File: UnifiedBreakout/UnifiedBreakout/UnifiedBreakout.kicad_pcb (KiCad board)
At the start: 2 copper layers, 307.3 x 121.9 mm, 95 parts, among them J1 24V DC IN, J10 MESA P2 INTERNAL IO, J11 MESA P3 REAR IO, J12 ENCODER IN, J13 ENCODER OUT, J14 ARGON J5, J15 ARGON J2.2, J16 RJ14, J17 RJ14, J18 RJ14, J19 RJ14, J2 ATX-24, J20 RJ14, J21 PENDANT, J22 DRAWBAR, J23 MIST, J24 AXIS PWR IN, J25 AXIS PWR OUT, J3 5V BUS, J4 24V BUS, J5 12V BUS, J7 RJ45, J8 RJ45, J9 RJ45, Q1 BC547, Q2 BC547, Q3 BC547, U1 4N35, U2 4N35, U3 4N35, U4 4N35, U5 4N35, U6 4N35, U7 74HC14

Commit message: Updated BOM
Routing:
- net +24V: vias 2 -> 1

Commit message: Final updates to unified BoB
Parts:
- C1, C3, C5, C7: footprint Capacitor_THT:C_Disc_D5.0mm_W2.5mm_P2.50mm -> Capacitor_THT:C_Disc_D5.0mm_W2.5mm_P5.00mm
- D5: value AXIS PWR -> LED
- D7: value DRAWBAR -> LED
- D9: value MIST -> LED
- R1, R10, R11, R12, R13, R14, R15, R16, R17, R18, R19, R2, R20, R21, R22, R23, R24, R25, R26, R27, R28, R29, R3, R30, R31, R4, R5, R6, R7, R8, R9: footprint Resistor_THT:R_Axial_DIN0207_L6.3mm_D2.5mm_P10.16mm_Horizontal -> Resistor_THT:R_Axial_DIN0207_L6.3mm_D2.5mm_P7.62mm_Horizontal
- moved R14 2.67 mm to (7.49, 139.4)
- moved R16 2.54 mm to (7.37, 155.2)
- moved R18 2.54 mm to (7.37, 171.4)
- moved R20 2.54 mm to (7.37, 203.7)
- moved R27 2.54 mm to (22.9, 136.9)
- moved R28 2.54 mm to (22.9, 152.7)
- moved R29 2.54 mm to (22.9, 168.9)
- moved R30 2.54 mm to (22.9, 201.2)
- moved R22 2.41 mm to (7.49, 188.2)
- moved R31 2.29 mm to (23.1, 185.7)
- moved J22 1.27 mm to (243.7, 114.3)
- moved J23 1.27 mm to (228.9, 114.3)
- moved J12 0.64 mm to (17.8, 116.2)
- moved J13 0.64 mm to (59.7, 116.2)
- moved J16 0.63 mm to (-8.76, 134.4)
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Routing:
- net +12V: track 308.9 -> 250.8 mm
- net +5V: track 511.8 -> 566.6 mm
- net GND: track 0.00 -> 53.2 mm
- net /ARGON ENCODER/B-: track 47.0 -> 58.1 mm, vias 3 -> 0
- net /SPINDLE_PWM_DIR: track 203.4 -> 210.8 mm
- net /ESTOP: track 226.8 -> 223.1 mm, vias 2 -> 1
- net Net-(D4-Pad2): track 8.67 -> 11.2 mm
- net Net-(D2-Pad2): track 4.07 -> 6.61 mm
- net /MIST RELAY/ENABLE: track 16.5 -> 19.1 mm
- net /DRAWBAR RELAY/ENABLE: track 17.0 -> 19.6 mm
- net /AXIS POWER RELAY/ENABLE: track 18.6 -> 21.2 mm
- net /ARGON ENCODER/A-: track 45.1 -> 47.6 mm
- net Net-(D6-Pad2): track 16.1 -> 18.5 mm
- net +5VP: track 370.2 -> 372.6 mm
- net /ATX_PWR: track 230.4 -> 228.1 mm
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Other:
- net class 12V net added: clearance 0.5, trace_width 2, via_dia 1.5, via_drill 1

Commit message: Generate gerbers
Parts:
- D5: value LED -> AXIS PWR
- D7: value LED -> DRAWBAR
- D9: value LED -> MIST
- ENCODER PWR SEL: renamed from JP1
- moved J24 1.27 mm to (233.2, 217.4)
- moved J25 1.27 mm to (208.8, 217.4)
- moved J22 1.02 mm to (243.7, 115.3)
- moved J23 1.02 mm to (228.9, 115.3)
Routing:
- net /L_OUT: track 26.2 -> 25.0 mm
- net /N_IN: track 18.1 -> 16.9 mm
- net /N_OUT: track 79.2 -> 78.0 mm
- net /L_IN: track 19.0 -> 17.9 mm
- net /MIST RELAY/IN_A: track 11.8 -> 10.8 mm
- net /DRAWBAR RELAY/IN_A: track 12.0 -> 11.0 mm
- net +12V: track 250.8 -> 249.8 mm

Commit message: Update big breakout board to Kicad nightly
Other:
- net class 12V net removed
- net class Default removed
- net class ESTOP removed
- net class Gnd removed
- net class High power removed
- net class Low power removed
- net class Mains removed

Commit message: WIP updating breakout for electrical enclosure
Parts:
- removed C1, C5: 100n, Capacitor_THT:C_Disc_D5.0mm_W2.5mm_P5.00mm
- removed C2, C6: 100uF, Capacitor_THT:CP_Radial_D8.0mm_P3.50mm
- removed D10, D8: 1N4001, Diode_THT:D_DO-41_SOD81_P10.16mm_Horizontal
- removed D3: ATX PWR GOOD, LED_THT:LED_D3.0mm
- removed D4: ATX STBY, LED_THT:LED_D3.0mm
- removed D7: DRAWBAR, LED_THT:LED_D3.0mm
- removed D9: MIST, LED_THT:LED_D3.0mm
- removed ENCODER PWR SEL: ENCODER PWR SEL, Connector_PinHeader_2.54mm:PinHeader_1x03_P2.54mm_Vertical
- removed J16, J17, J18, J19, J20: RJ14, Wurth:615004141121
- removed J22: DRAWBAR, Connector_Phoenix_MSTB:PhoenixContact_MSTBA_2,5_2-G-5,08_1x02_P5.08mm_Horizontal
- removed J23: MIST, Connector_Phoenix_MSTB:PhoenixContact_MSTBA_2,5_2-G-5,08_1x02_P5.08mm_Horizontal
- removed J3: 5V BUS, Connector_Phoenix_MSTB:PhoenixContact_MSTBA_2,5_2-G-5,08_1x02_P5.08mm_Horizontal
- removed J5: 12V BUS, Connector_Phoenix_MSTB:PhoenixContact_MSTBA_2,5_2-G-5,08_1x02_P5.08mm_Horizontal
- removed Q3: BC547, Package_TO_SOT_THT:TO-92_Inline_Wide
- removed R11, R13: 680R, Resistor_THT:R_Axial_DIN0207_L6.3mm_D2.5mm_P7.62mm_Horizontal
- removed R12: 2K2, Resistor_THT:R_Axial_DIN0207_L6.3mm_D2.5mm_P7.62mm_Horizontal
- removed R25: 10K, Resistor_THT:R_Axial_DIN0207_L6.3mm_D2.5mm_P7.62mm_Horizontal
- removed RL2, RL3: JW2, Relay_THT:Relay_DPDT_Panasonic_JW2
- added Q4: 2N7000, Package_TO_SOT_THT:TO-92_Inline, F.Cu at (89.7, 82.3)
- added U9: 4N35, Package_DIP:DIP-6_W7.62mm, F.Cu at (162.8, 86.4)
- D5: value AXIS PWR -> LED
- J1: value 24V DC IN -> DRAWBAR+MIST; footprint SwitchCraft-BarrelJack-RAPC722BK:RAPC722BK -> Connector_Phoenix_MSTB:PhoenixContact_MSTBA_2,5_2-G-5,08_1x02_P5.08mm_Horizontal
- J2: value ATX-24 -> Screw_Terminal_01x05; footprint Connector_Molex:Molex_Mini-Fit_Jr_5569-24A2_2x12_P4.20mm_Horizontal -> Connector_Phoenix_MSTB:PhoenixContact_MSTBA_2,5_5-G-5,08_1x05_P5.08mm_Horizontal
- Q1: footprint Package_TO_SOT_THT:TO-92_Inline_Wide -> Package_TO_SOT_THT:TO-92_Inline
- Q2: value BC547 -> 2N7000; footprint Package_TO_SOT_THT:TO-92_Inline_Wide -> Package_TO_SOT_THT:TO-92_Inline
- R1, R10: value 2K2 -> 10K
- R4: value 220R -> 2K2
- R5: value 220R -> 220K
- moved J2 429.3 mm to (-149.9, 162.6), turned to 0 degrees
- moved J24 234.8 mm to (47.9, 73.2)
- moved H6 227.1 mm to (63.2, 65.8)
- moved C4 219.7 mm to (81.2, 78.0), turned to 0 degrees
- moved J4 218.6 mm to (71.1, 132.1), turned to 180 degrees
- moved J1 218.6 mm to (58.4, 165.1), turned to 0 degrees
- moved H3 209.8 mm to (55.2, 57.8)
- moved J25 206.7 mm to (47.9, 87.7)
- moved C3 206.0 mm to (79.5, 94.4), turned to 0 degrees
- moved R1 205.1 mm to (68.7, 75.3), turned to 0 degrees
- moved H4 205.0 mm to (55.2, 65.8)
- moved J15 203.5 mm to (12.2, 72.9)
- moved R22 169.9 mm to (149.9, 95.6)
- moved U6 169.5 mm to (149.9, 86.4)
- moved R20 168.9 mm to (137.0, 95.6)
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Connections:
- net /X MOT/DIR renamed /MESA P3 REAR IO/IO_04_STEPGEN_00_DIR
- net /Y MOT/DIR renamed /MESA P3 REAR IO/IO_08_STEPGEN_01_DIR
- net /Z MOT/DIR renamed /MESA P3 REAR IO/IO_10_STEPGEN_02_DIR
- D5 pad 2: +12V -> +24V
- D6 pad 1: +12V -> +24V
- J1 pad 1: +24V -> Net-(J1-Pin_1)
- J1 pad 2: GND -> Net-(J1-Pin_2)
- J10 pad 3: /ATX_PWR -> /TOOL_PROBE
- J12 pad 0: GND -> (no net)
- J12 pad 1: Net-(J12-Pad1) -> unconnected-(J12-Pad1)
- J12 pad 11: Net-(J12-Pad11) -> unconnected-(J12-P111-Pad11)
- J12 pad 12: Net-(J12-Pad12) -> unconnected-(J12-P12-Pad12)
- J12 pad 13: Net-(J12-Pad13) -> unconnected-(J12-P13-Pad13)
- J12 pad 2: Net-(J12-Pad2) -> unconnected-(J12-Pad2)
- J12 pad 3: Net-(J12-Pad3) -> unconnected-(J12-Pad3)
- J12 pad 4: Net-(J12-Pad4) -> unconnected-(J12-Pad4)
- J12 pad 9: Net-(J12-Pad9) -> Net-(J12-P9)
- J13 pad 0: GND -> (no net)
- J13 pad 1: Net-(J13-Pad1) -> unconnected-(J13-Pad1)
- J13 pad 11: Net-(J13-Pad11) -> unconnected-(J13-P111-Pad11)
- J13 pad 12: Net-(J13-Pad12) -> unconnected-(J13-P12-Pad12)
- J13 pad 13: Net-(J13-Pad13) -> unconnected-(J13-P13-Pad13)
- J13 pad 2: Net-(J13-Pad2) -> unconnected-(J13-Pad2)
- J13 pad 3: Net-(J13-Pad3) -> unconnected-(J13-Pad3)
- J13 pad 4: Net-(J13-Pad4) -> unconnected-(J13-Pad4)
- J13 pad 9: /ARGON ENCODER/ARGON5V -> Net-(J12-P9)
- J14 pad 10: Net-(J14-Pad10) -> unconnected-(J14-Pin_10-Pad10)
- J14 pad 11: Net-(J14-Pad11) -> unconnected-(J14-Pin_11-Pad11)
- J14 pad 12: Net-(J14-Pad12) -> unconnected-(J14-Pin_12-Pad12)
- J14 pad 13: Net-(J14-Pad13) -> unconnected-(J14-Pin_13-Pad13)
- J14 pad 14: Net-(J14-Pad14) -> unconnected-(J14-Pin_14-Pad14)
- J14 pad 17: Net-(J14-Pad17) -> unconnected-(J14-Pin_17-Pad17)
- J14 pad 18: Net-(J14-Pad18) -> unconnected-(J14-Pin_18-Pad18)
- J14 pad 19: Net-(J14-Pad19) -> unconnected-(J14-Pin_19-Pad19)
- J14 pad 2: Net-(J14-Pad2) -> unconnected-(J14-Pin_2-Pad2)
- J14 pad 20: Net-(J14-Pad20) -> unconnected-(J14-Pin_20-Pad20)
- J14 pad 21: Net-(J14-Pad21) -> unconnected-(J14-Pin_21-Pad21)
- J14 pad 22: Net-(J14-Pad22) -> unconnected-(J14-Pin_22-Pad22)
- J14 pad 23: Net-(J14-Pad23) -> unconnected-(J14-Pin_23-Pad23)
- J14 pad 24: Net-(J14-Pad24) -> unconnected-(J14-Pin_24-Pad24)
- J14 pad 25: Net-(J14-Pad25) -> unconnected-(J14-Pin_25-Pad25)
- J14 pad 26: Net-(J14-Pad26) -> unconnected-(J14-Pin_26-Pad26)
- J14 pad 3: Net-(J14-Pad3) -> unconnected-(J14-Pin_3-Pad3)
- J14 pad 5: Net-(J14-Pad5) -> unconnected-(J14-Pin_5-Pad5)
- J14 pad 7: Net-(J14-Pad7) -> unconnected-(J14-Pin_7-Pad7)
- J14 pad 8: Net-(J14-Pad8) -> unconnected-(J14-Pin_8-Pad8)
- J14 pad 9: Net-(J14-Pad9) -> unconnected-(J14-Pin_9-Pad9)
- J15 pad 2: Net-(J15-Pad2) -> unconnected-(J15-Pad2)
- J2 pad 1: Net-(J2-Pad1) -> /LIM X/INPUT
- J2 pad 2: Net-(J2-Pad1) -> /LIM Y/INPUT
- J2 pad 3: GND -> /LIM Z/INPUT
- J2 pad 4: +5V -> /PROBE/INPUT
- J2 pad 5: GND -> /TOOL_PROBE/INPUT
- J21 pad 10: Net-(J21-Pad10) -> unconnected-(J21-Pad10)
- J21 pad 13: Net-(J21-Pad13) -> unconnected-(J21-Pad13)
- J21 pad 17: Net-(J21-Pad17) -> unconnected-(J21-P17-Pad17)
- J21 pad 18: Net-(J21-Pad18) -> unconnected-(J21-P18-Pad18)
- J21 pad 22: Net-(J21-Pad22) -> unconnected-(J21-P22-Pad22)
- J21 pad 23: Net-(J21-Pad23) -> unconnected-(J21-P23-Pad23)
- J21 pad 24: Net-(J21-Pad24) -> unconnected-(J21-P24-Pad24)
- J21 pad 6: Net-(J21-Pad6) -> unconnected-(J21-Pad6)
- J21 pad 7: Net-(J21-Pad7) -> unconnected-(J21-Pad7)
- J21 pad 8: Net-(J21-Pad8) -> unconnected-(J21-Pad8)
- J21 pad 9: Net-(J21-Pad9) -> unconnected-(J21-Pad9)
- Q2 pad 1: Net-(D8-Pad2) -> GND
- Q2 pad 2: Net-(Q2-Pad2) -> Net-(Q2-G)
- Q2 pad 3: GND -> Net-(J1-Pin_1)
- R1 pad 1: Net-(J2-Pad9) -> +5VP
- R1 pad 2: /ATX_PWR -> /DRAWBAR_VALVE
- R10 pad 1: Net-(Q2-Pad2) -> +5VP
- R10 pad 2: /DRAWBAR RELAY/ENABLE -> /TOOL_PROBE
- R4 pad 2: Net-(J2-Pad8) -> GND
- R5 pad 1: Net-(J2-Pad9) -> Net-(R5-Pad1)
- R5 pad 2: Net-(D4-Pad2) -> GND
- RL1 pad 1: +12V -> +24V
- RL1 pad 2: Net-(RL1-Pad2) -> unconnected-(RL1-Pad2)
- RL1 pad 7: Net-(RL1-Pad7) -> unconnected-(RL1-Pad7)
- U1 pad 3: Net-(U1-Pad3) -> unconnected-(U1-NC-Pad3)
- U2 pad 1: Net-(J16-Pad4) -> /LIM X/INPUT
- U2 pad 3: Net-(U2-Pad3) -> unconnected-(U2-NC-Pad3)
- U3 pad 1: Net-(J17-Pad4) -> /LIM Y/INPUT
- U3 pad 3: Net-(U3-Pad3) -> unconnected-(U3-NC-Pad3)
- U4 pad 1: Net-(J18-Pad4) -> /LIM Z/INPUT
- U4 pad 3: Net-(U4-Pad3) -> unconnected-(U4-NC-Pad3)
- U5 pad 1: Net-(J19-Pad4) -> /PROBE/INPUT
- U5 pad 3: Net-(U5-Pad3) -> unconnected-(U5-NC-Pad3)
- U6 pad 1: Net-(J20-Pad4) -> /DRAWBAR SW/INPUT
- U6 pad 3: Net-(U6-Pad3) -> unconnected-(U6-NC-Pad3)
- U7 pad 10: (no net) -> unconnected-(U7-Pad10)
- U7 pad 11: (no net) -> unconnected-(U7-Pad11)
- U7 pad 12: (no net) -> unconnected-(U7-Pad12)
- U7 pad 13: (no net) -> unconnected-(U7-Pad13)
- U7 pad 4: /DRAWBAR RELAY/ENABLE -> Net-(Q2-G)
- U7 pad 6: /MIST RELAY/ENABLE -> Net-(Q4-G)
- U7 pad 8: (no net) -> unconnected-(U7-Pad8)
- U7 pad 9: (no net) -> unconnected-(U7-Pad9)
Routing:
- net +24V: track 702.6 -> 0.00 mm, vias 1 -> 0
- net +5V: track 566.6 -> 0.00 mm
- net +5VP: track 372.6 -> 0.00 mm
- net +12V: track 249.8 -> 0.00 mm
- net /ATX_PWR: track 228.1 -> 0.00 mm, vias 4 -> 0
- net /ESTOP: track 223.1 -> 0.00 mm, vias 1 -> 0
- net /SPINDLE_PWM_DIR: track 210.8 -> 0.00 mm
- net /SPINDLE_STEPGEN_DIR: track 208.7 -> 0.00 mm
- net /SPINDLE_STEPGEN_STEP: track 206.6 -> 0.00 mm
- net /ALARM: track 198.4 -> 0.00 mm
- net /SPINDLE_PWM_SIG: track 192.2 -> 0.00 mm
- net /MESA P3 REAR IO/IO_04_STEPGEN_00_DIR: track 178.9 -> 0.00 mm
- net /MESA P3 REAR IO/IO_02_STEPGEN_00_STEP: track 178.3 -> 0.00 mm
- net /MESA P3 REAR IO/IO_06_STEPGEN_01_STEP: track 163.5 -> 0.00 mm
- net /SPINDLE_ENC_IDX: track 163.3 -> 0.00 mm
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- removed copper zone on B.Cu, net GND
- removed copper zone on F.Cu, net GND
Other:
- board size 307.3 x 121.9 mm -> 200 x 100 mm
- board text removed: "+"
- board text removed: "ARGON"
- board text removed: "DRAWBAR"
- board text removed: "L"
- board text removed: "LIMIT X"
- board text removed: "LIMIT Y"
- board text removed: "LIMIT Z"
- board text removed: "MESA"
- board text removed: "N"
- board text removed: "PE"
- board text removed: "PROBE"
- board text removed: "PWM"
- board text removed: "SPINDLE SOURCE"
- board text removed: "STEPGEN"
- board text removed: "X AXIS"
- board text removed: "Y AXIS"
- board text removed: "Z AXIS"

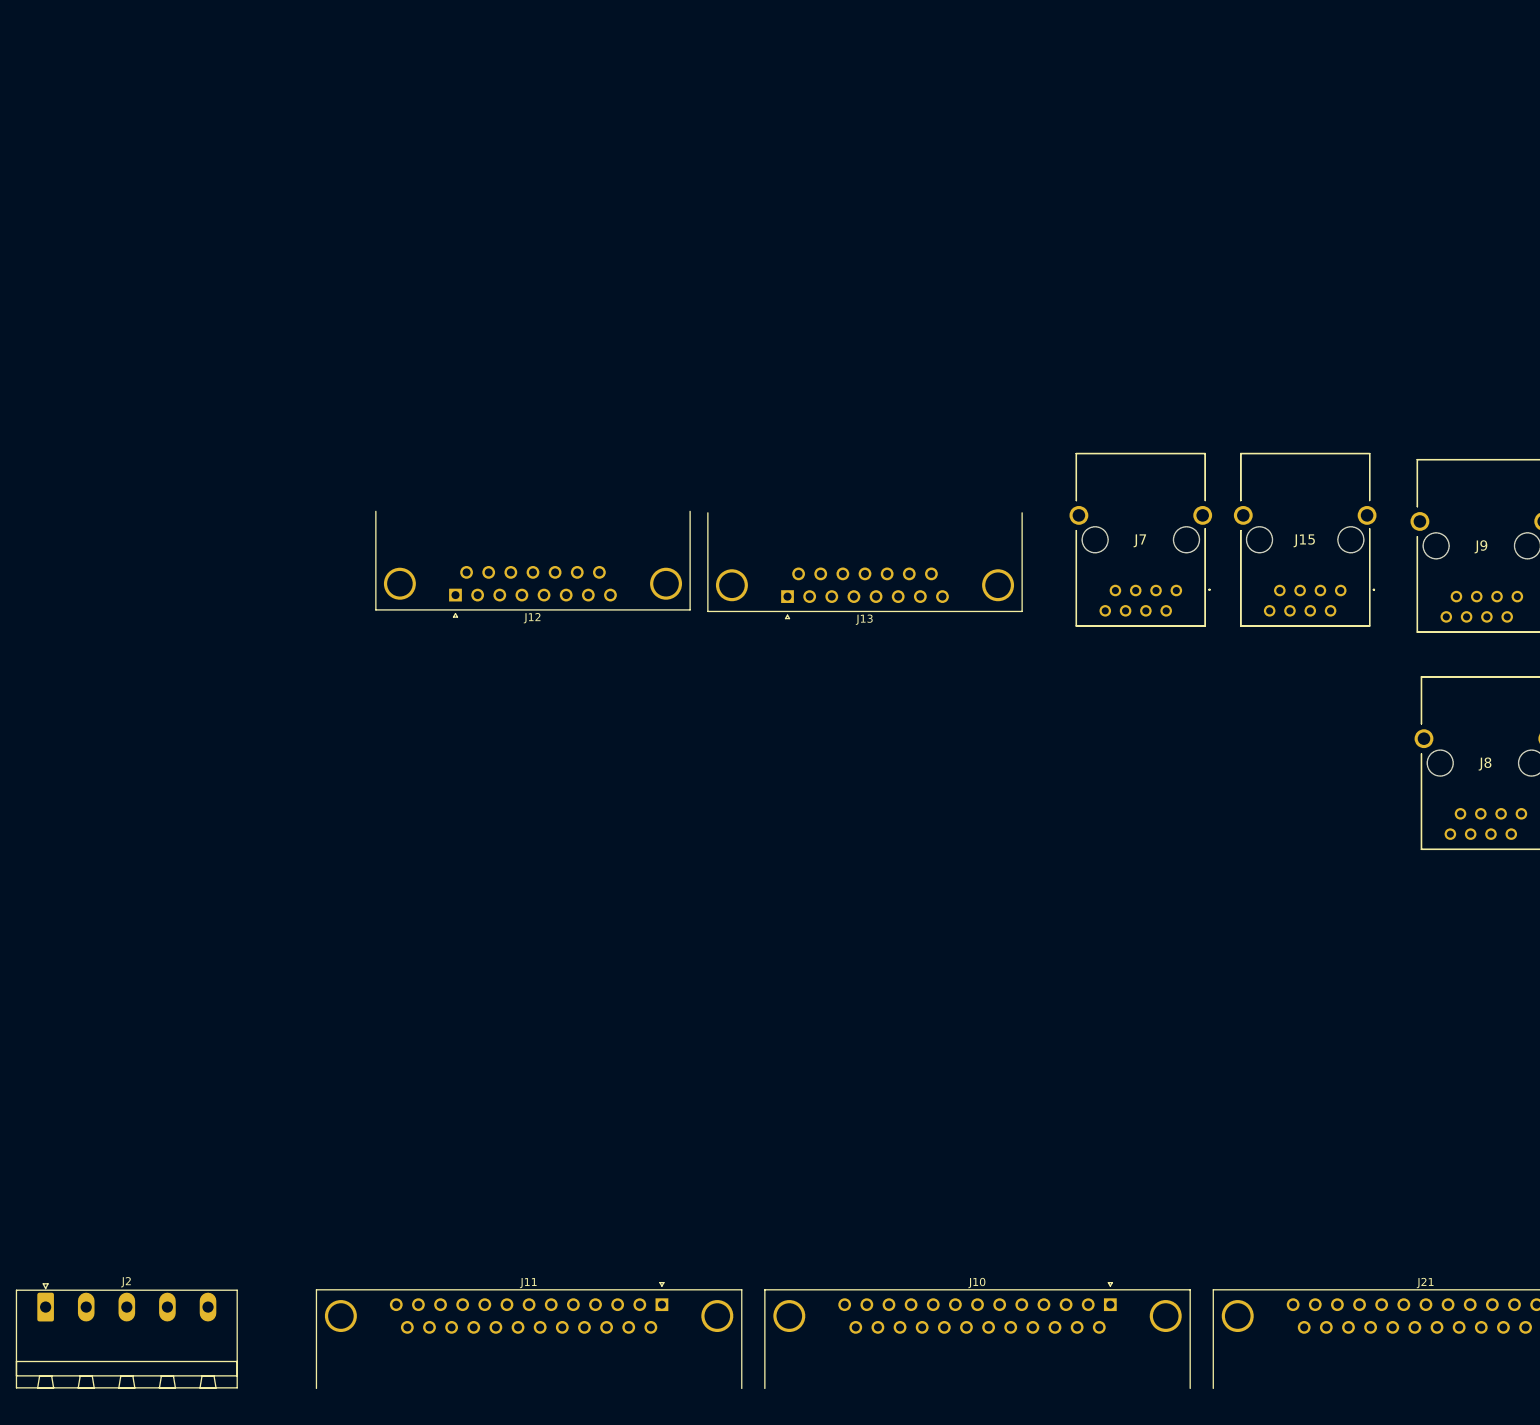
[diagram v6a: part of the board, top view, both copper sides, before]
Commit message: Add stacked DA15 part
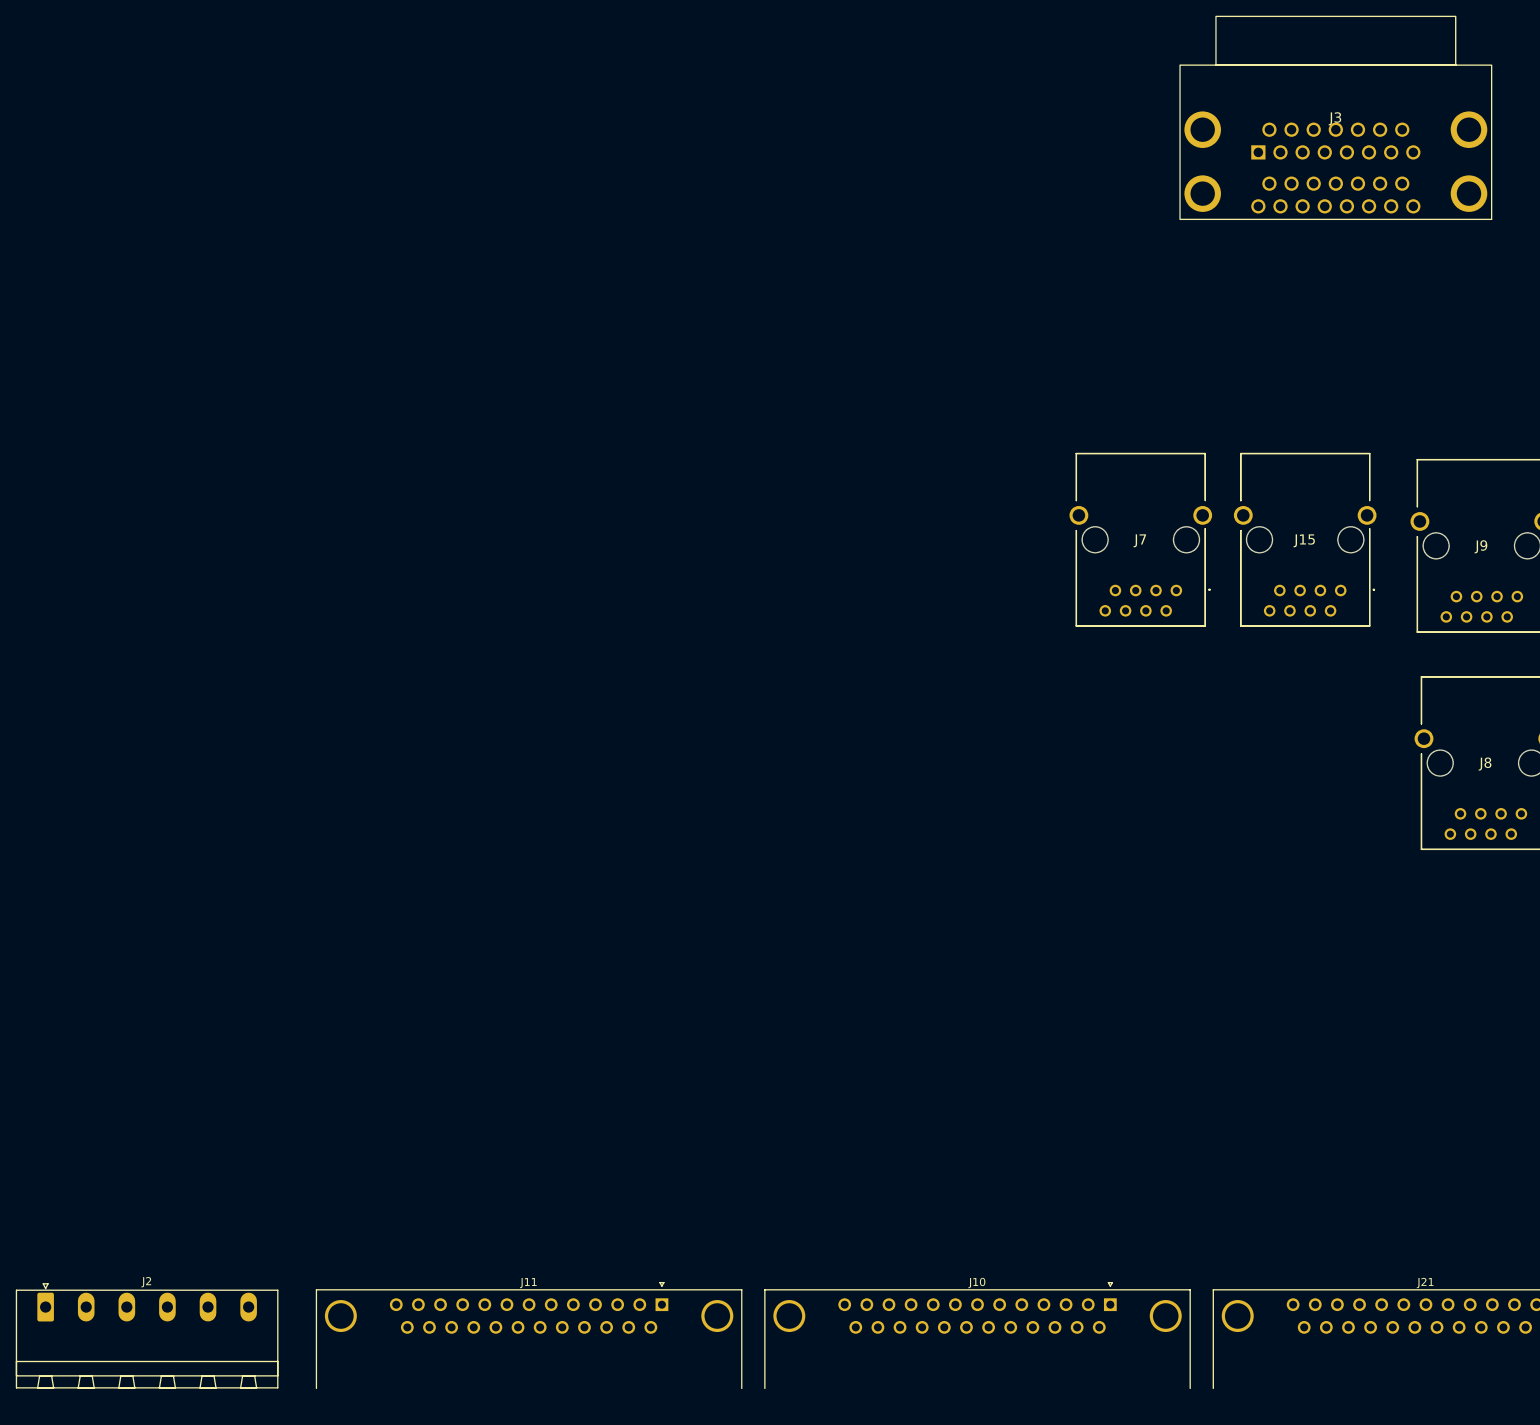
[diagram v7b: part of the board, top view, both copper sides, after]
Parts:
- removed J12: ENCODER IN, Connector_Dsub:DSUB-15_Female_Horizontal_P2.77x2.84mm_EdgePinOffset7.70mm_Housed_MountingHolesOffset9.12mm
- removed J13: ENCODER OUT, Connector_Dsub:DSUB-15_Female_Horizontal_P2.77x2.84mm_EdgePinOffset7.70mm_Housed_MountingHolesOffset9.12mm
- added J3: Dual DA15 Stacked, UnifiedBreakout:NorComp-Dual-DA15, F.Cu at (1.89, 18.1)
- J2: footprint Connector_Phoenix_MSTB:PhoenixContact_MSTBA_2,5_5-G-5,08_1x05_P5.08mm_Horizontal -> Connector_Phoenix_MSTB:PhoenixContact_MSTBA_2,5_6-G-5,08_1x06_P5.08mm_Horizontal

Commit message: Add dual level DB25
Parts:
- removed J10: MESA P2 INTERNAL IO, Connector_Dsub:DSUB-25_Female_Horizontal_P2.77x2.84mm_EdgePinOffset7.70mm_Housed_MountingHolesOffset9.12mm
- removed J11: MESA P3 REAR IO, Connector_Dsub:DSUB-25_Female_Horizontal_P2.77x2.84mm_EdgePinOffset7.70mm_Housed_MountingHolesOffset9.12mm
- added J5: DB25_Receptacle_Dual, UnifiedBreakout:NorComp-Dual-DB25, F.Cu at (-17.0, 117.4)
- J14: footprint Connector_IDC:IDC-Header_2x13_P2.54mm_Horizontal -> Connector_IDC:IDC-Header_2x13_P2.54mm_Vertical
